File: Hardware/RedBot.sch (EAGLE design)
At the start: 64 parts, among them U1 ATMEGA328P, U2 TB6612FNG, U3 MIC5219 5V, U4 MIC5219 3.3V, U5 FT232RLSSOP, U6 7408SE, Y1 16MHz

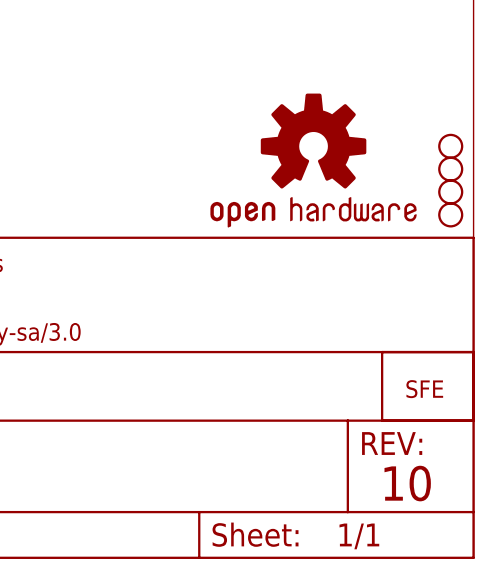
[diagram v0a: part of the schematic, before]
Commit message: Production readied
add fiducials & create panel
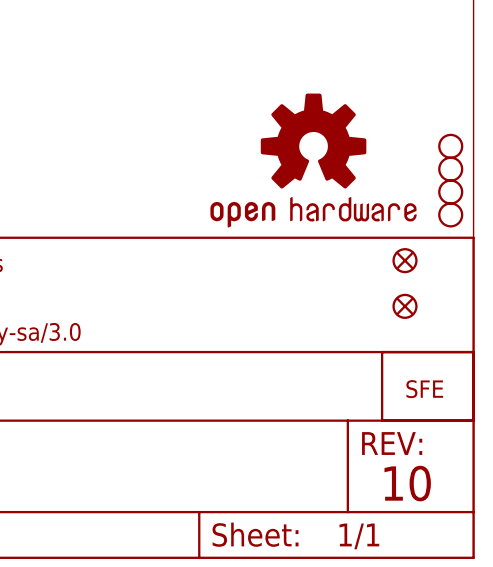
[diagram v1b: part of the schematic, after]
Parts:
- added FID1, FID2: FIDUCIALUFIDUCIAL, SparkFun-Aesthetics:FIDUCIALUFIDUCIAL
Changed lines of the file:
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@@
 <part name="U$20" library="SparkFun-Aesthetics" deviceset="5V" device=""/>
 <part name="U$21" library="SparkFun-Aesthetics" deviceset="FOUR_LAYER_WARNING" device=""/>
+<part name="FID1" library="SparkFun-Aesthetics" deviceset="FIDUCIAL" device="UFIDUCIAL"/>
+<part name="FID2" library="SparkFun-Aesthetics" deviceset="FIDUCIAL" device="UFIDUCIAL"/>
 </parts>
 <sheets>
@@
 <instance part="U$20" gate="G$1" x="127" y="165.1"/>
 <instance part="U$21" gate="G$1" x="304.8" y="36.068"/>
+<instance part="FID1" gate="G$1" x="398.78" y="33.02"/>
+<instance part="FID2" gate="G$1" x="398.78" y="27.94"/>
 </instances>
 <busses>

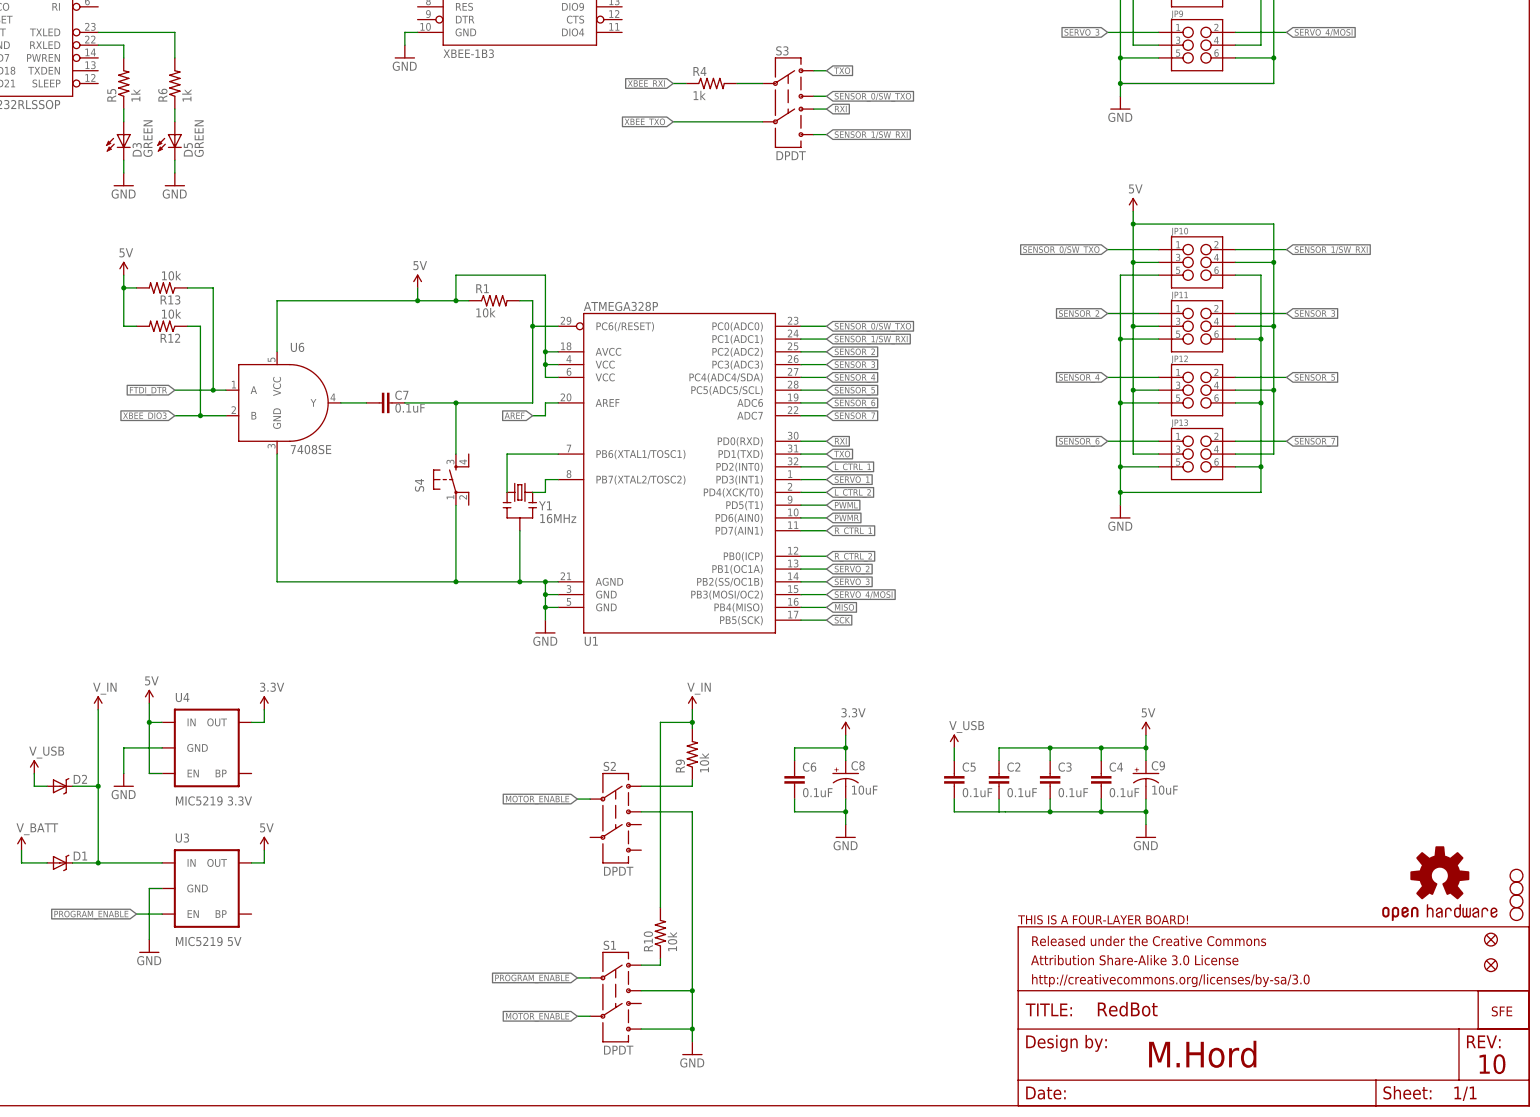
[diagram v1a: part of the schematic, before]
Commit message: Fix polarity issue on FT232 LEDs
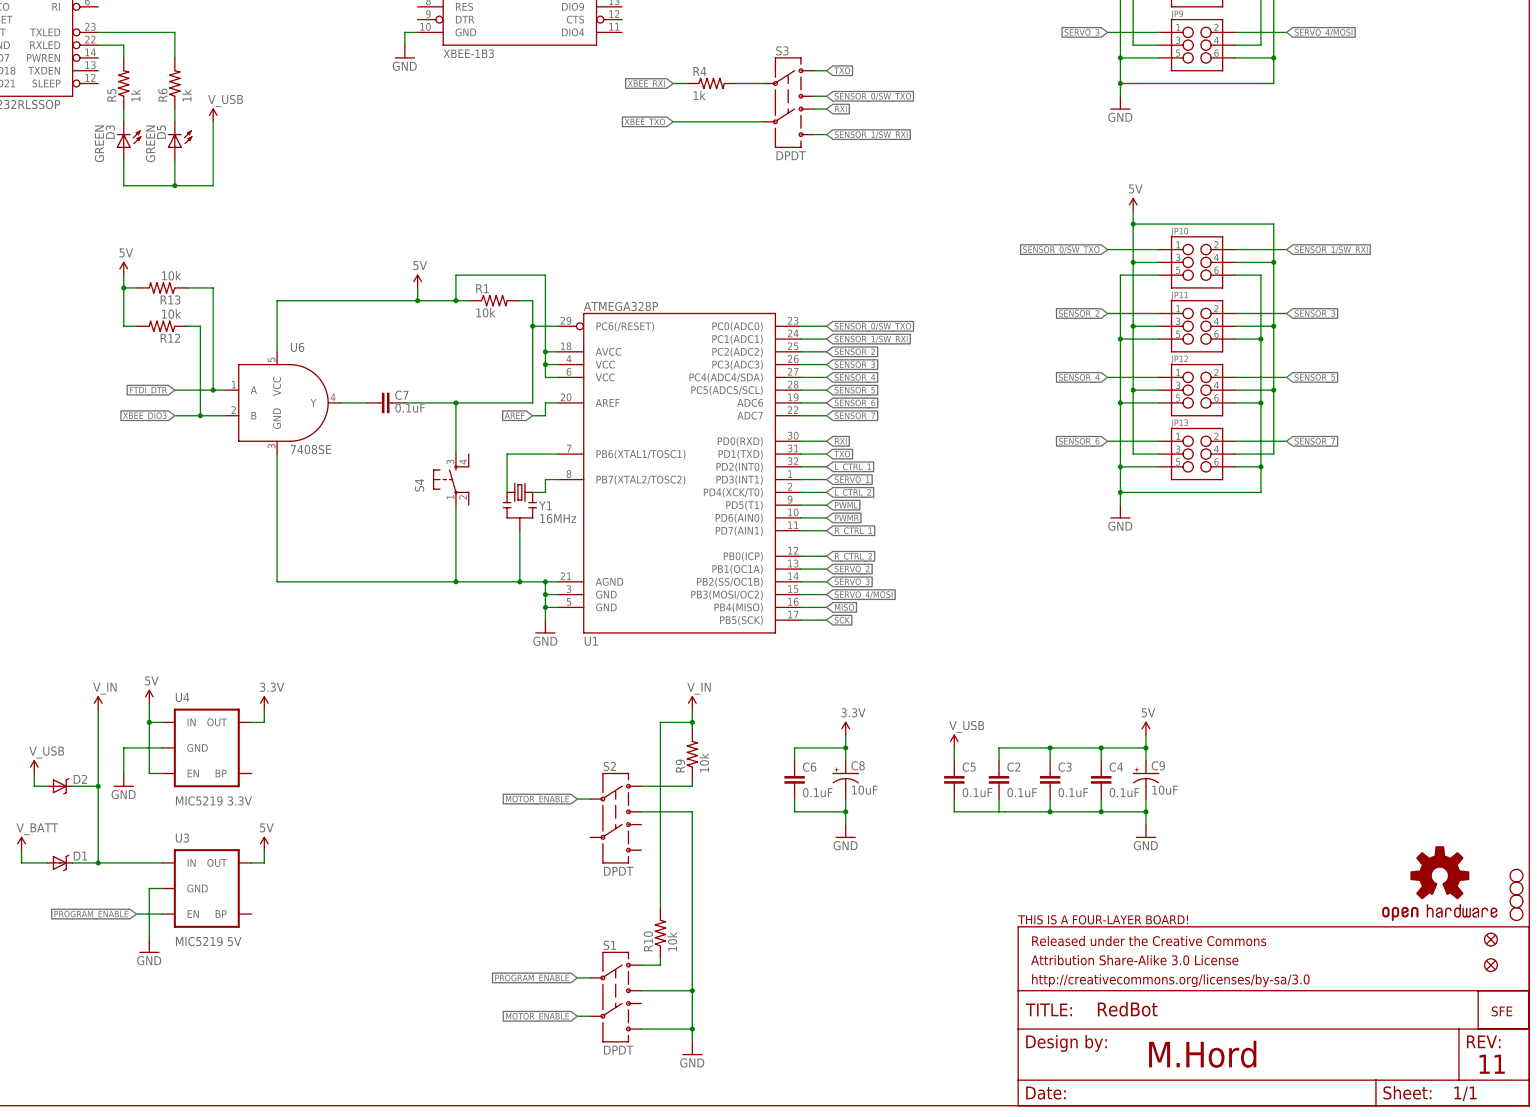
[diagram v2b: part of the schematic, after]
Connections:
- net GND: no longer D3.C, D5.C
- net N$3: now also D5.C; no longer D5.A
- net N$4: now also D3.C; no longer D3.A
- net V_USB: now also D3.A, D5.A
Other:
- note added: "11"
- note removed: "10"
- moved on the sheet: D3, D5
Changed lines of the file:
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@@
 <attribute name="VALUE" value="GREEN"/>
 </part>
-<part name="GND12" library="SparkFun-Aesthetics" deviceset="GND" device=""/>
-<part name="GND13" library="SparkFun-Aesthetics" deviceset="GND" device=""/>
 <part name="JP5" library="SparkFun-Connectors" deviceset="AVR_SPI_PRG_6" device="PTH" value="AVR_SPI_PRG_6PTH"/>
 <part name="GND15" library="SparkFun-Aesthetics" deviceset="GND" device=""/>
@@
 <part name="FID1" library="SparkFun-Aesthetics" deviceset="FIDUCIAL" device="UFIDUCIAL"/>
 <part name="FID2" library="SparkFun-Aesthetics" deviceset="FIDUCIAL" device="UFIDUCIAL"/>
+<part name="U$22" library="SparkFun-Aesthetics" deviceset="5V" device="" value="V_USB"/>
 </parts>
 <sheets>
@@
 <wire x1="0" y1="254" x2="0" y2="0" width="0.1524" layer="94"/>
 <text x="330.2" y="7.62" size="5.08" layer="94">M.Hord</text>
-<text x="395.986" y="6.35" size="3.81" layer="94">10</text>
+<text x="395.986" y="6.35" size="3.81" layer="94">11</text>
 </plain>
 <instances>
@@
 <instance part="U$10" gate="G$1" x="185.42" y="162.56"/>
 <instance part="S4" gate="S" x="193.04" y="124.46" rot="R90"/>
-<instance part="D3" gate="G$1" x="127" y="193.04"/>
+<instance part="D3" gate="G$1" x="127" y="190.5" rot="R180"/>
 <instance part="D4" gate="G$1" x="35.56" y="243.84" rot="R90"/>
 <instance part="R5" gate="G$1" x="127" y="203.2" rot="R90"/>
 <instance part="R6" gate="G$1" x="137.16" y="203.2" rot="R90"/>
 <instance part="R7" gate="G$1" x="25.4" y="243.84" rot="R180"/>
-<instance part="D5" gate="G$1" x="137.16" y="193.04"/>
-<instance part="GND12" gate="1" x="137.16" y="182.88"/>
-<instance part="GND13" gate="1" x="127" y="182.88"/>
+<instance part="D5" gate="G$1" x="137.16" y="190.5" rot="R180"/>
 <instance part="JP5" gate="G$1" x="27.94" y="205.74" smashed="yes">
 <attribute name="NAME" x="23.622" y="211.582" size="1.778" layer="95"/>
@@
 <instance part="FID1" gate="G$1" x="398.78" y="33.02"/>
 <instance part="FID2" gate="G$1" x="398.78" y="27.94"/>
+<instance part="U$22" gate="G$1" x="144.78" y="195.58"/>
 </instances>
 <busses>
@@
 </segment>
 <segment>
-<pinref part="D3" gate="G$1" pin="C"/>
-<pinref part="GND13" gate="1" pin="GND"/>
-<wire x1="127" y1="187.96" x2="127" y2="185.42" width="0.1524" layer="91"/>
-</segment>
-<segment>
-<pinref part="D5" gate="G$1" pin="C"/>
-<pinref part="GND12" gate="1" pin="GND"/>
-<wire x1="137.16" y1="187.96" x2="137.16" y2="185.42" width="0.1524" layer="91"/>
-</segment>
-<segment>
 <pinref part="JP5" gate="G$1" pin="6"/>
 <wire x1="38.1" y1="203.2" x2="40.64" y2="203.2" width="0.1524" layer="91"/>
@@
 <wire x1="292.1" y1="71.12" x2="292.1" y2="68.58" width="0.1524" layer="91"/>
 </segment>
+<segment>
+<pinref part="D3" gate="G$1" pin="A"/>
+<wire x1="127" y1="187.96" x2="127" y2="182.88" width="0.1524" layer="91"/>
+<pinref part="D5" gate="G$1" pin="A"/>
+<wire x1="127" y1="182.88" x2="137.16" y2="182.88" width="0.1524" layer="91"/>
+<wire x1="137.16" y1="182.88" x2="137.16" y2="187.96" width="0.1524" layer="91"/>
+<pinref part="U$22" gate="G$1" pin="5V"/>
+<wire x1="137.16" y1="182.88" x2="144.78" y2="182.88" width="0.1524" layer="91"/>
+<wire x1="144.78" y1="182.88" x2="144.78" y2="195.58" width="0.1524" layer="91"/>
+<junction x="137.16" y="182.88"/>
+</segment>
 </net>
 <net name="PROGRAM_ENABLE" class="0">
@@
 <wire x1="210.82" y1="137.16" x2="208.28" y2="137.16" width="0.1524" layer="91"/>
 <label x="208.28" y="137.16" size="1.27" layer="95" rot="R180" xref="yes"/>
-</segment>
-</net>
-<net name="N$3" class="0">
-<segment>
-<pinref part="R6" gate="G$1" pin="1"/>
-<pinref part="D5" gate="G$1" pin="A"/>
-<wire x1="137.16" y1="198.12" x2="137.16" y2="195.58" width="0.1524" layer="91"/>
-</segment>
-</net>
-<net name="N$4" class="0">
-<segment>
-<pinref part="R5" gate="G$1" pin="1"/>
-<pinref part="D3" gate="G$1" pin="A"/>
-<wire x1="127" y1="198.12" x2="127" y2="195.58" width="0.1524" layer="91"/>
 </segment>
 </net>
@@
 </segment>
 </net>
+<net name="N$3" class="0">
+<segment>
+<pinref part="D5" gate="G$1" pin="C"/>
+<pinref part="R6" gate="G$1" pin="1"/>
+<wire x1="137.16" y1="195.58" x2="137.16" y2="198.12" width="0.1524" layer="91"/>
+</segment>
+</net>
+<net name="N$4" class="0">
+<segment>
+<pinref part="R5" gate="G$1" pin="1"/>
+<pinref part="D3" gate="G$1" pin="C"/>
+<wire x1="127" y1="198.12" x2="127" y2="195.58" width="0.1524" layer="91"/>
+</segment>
+</net>

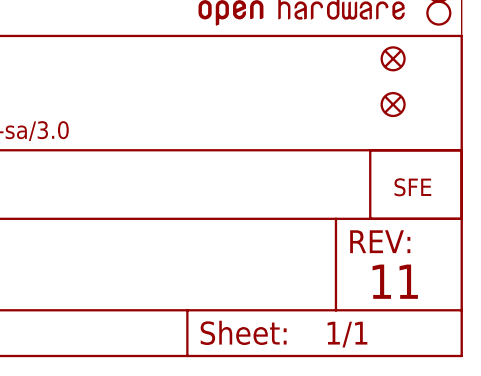
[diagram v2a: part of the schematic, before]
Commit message: Update parts to 0603
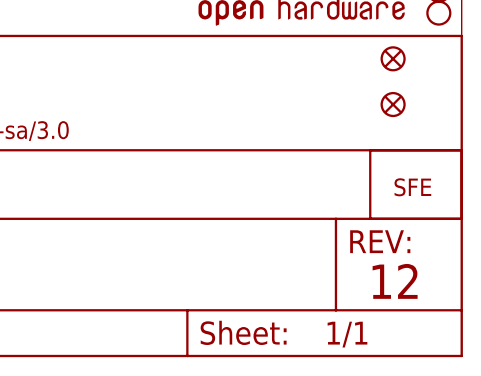
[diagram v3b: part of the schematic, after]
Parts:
- C2, C3, C4, C5, C6, C7: device SparkFun-Capacitors:.1UF-CER -> SparkFun-Capacitors:0.1UF-25V(+80/-20%)(0603)
- R1: device SparkFun-Resistors:10KOHM1/10W1%(0603) -> SparkFun-Resistors:10KOHM1/10W1%(0603)0603
- R10, R11, R12, R13, R9: device SparkFun-Resistors:10KOHM1/10W1%(0603) -> SparkFun-Resistors:10KOHM1/10W1%(0603)0603; VALUE 10k -> (none)
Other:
- note added: "12"
- note removed: "11"
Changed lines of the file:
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@@
 <part name="FRAME1" library="SparkFun-Aesthetics" deviceset="FRAME-LETTER" device=""/>
 <part name="U1" library="SparkFun-DigitalIC" deviceset="ATMEGA328_SMT" device="" value="ATMEGA328P"/>
-<part name="C2" library="SparkFun-Capacitors" deviceset=".1UF-CER" device="" value="0.1uF"/>
-<part name="C3" library="SparkFun-Capacitors" deviceset=".1UF-CER" device="" value="0.1uF"/>
-<part name="R1" library="SparkFun-Resistors" deviceset="10KOHM1/10W1%(0603)" device="" value="10k"/>
+<part name="C2" library="SparkFun-Capacitors" deviceset="0.1UF-25V(+80/-20%)(0603)" device="" value="0.1uF"/>
+<part name="C3" library="SparkFun-Capacitors" deviceset="0.1UF-25V(+80/-20%)(0603)" device="" value="0.1uF"/>
+<part name="R1" library="SparkFun-Resistors" deviceset="10KOHM1/10W1%(0603)" device="0603" value="10k"/>
 <part name="U5" library="SparkFun-DigitalIC" deviceset="FT232RL" device="SSOP"/>
 <part name="U2" library="SparkFun-PowerIC" deviceset="TB6621FNG" device="" value="TB6612FNG"/>
 <part name="JP3" library="SparkFun-Connectors" deviceset="POWER_JACK" device="SMD" value="5.5x2.1mm Barrel"/>
-<part name="C4" library="SparkFun-Capacitors" deviceset=".1UF-CER" device="" value="0.1uF"/>
-<part name="C5" library="SparkFun-Capacitors" deviceset=".1UF-CER" device="" value="0.1uF"/>
-<part name="C6" library="SparkFun-Capacitors" deviceset=".1UF-CER" device="" value="0.1uF"/>
+<part name="C4" library="SparkFun-Capacitors" deviceset="0.1UF-25V(+80/-20%)(0603)" device="" value="0.1uF"/>
+<part name="C5" library="SparkFun-Capacitors" deviceset="0.1UF-25V(+80/-20%)(0603)" device="" value="0.1uF"/>
+<part name="C6" library="SparkFun-Capacitors" deviceset="0.1UF-25V(+80/-20%)(0603)" device="" value="0.1uF"/>
 <part name="S1" library="SparkFun-Electromechanical" deviceset="SWITCH-DPDT" device="AYZ0202" value="DPDT"/>
 <part name="S2" library="SparkFun-Electromechanical" deviceset="SWITCH-DPDT" device="AYZ0202" value="DPDT"/>
@@
 <part name="GND11" library="SparkFun-Aesthetics" deviceset="GND" device=""/>
 <part name="U$9" library="SparkFun-Aesthetics" deviceset="5V" device=""/>
-<part name="C7" library="SparkFun-Capacitors" deviceset=".1UF-CER" device="" value="0.1uF">
+<part name="C7" library="SparkFun-Capacitors" deviceset="0.1UF-25V(+80/-20%)(0603)" device="" value="0.1uF">
 <attribute name="PROD_ID" value="CAP-00810"/>
 <attribute name="VALUE" value="0.1uF"/>
@@
 <part name="U$13" library="SparkFun-Aesthetics" deviceset="5V" device=""/>
 <part name="V_IN1" library="SparkFun-Aesthetics" deviceset="5V" device="" value="V_IN"/>
-<part name="R9" library="SparkFun-Resistors" deviceset="10KOHM1/10W1%(0603)" device="" value="10k">
+<part name="R9" library="SparkFun-Resistors" deviceset="10KOHM1/10W1%(0603)" device="0603" value="10k">
 <attribute name="PROD_ID" value="RES-00824"/>
-<attribute name="VALUE" value="10k"/>
 </part>
-<part name="R10" library="SparkFun-Resistors" deviceset="10KOHM1/10W1%(0603)" device="" value="10k">
+<part name="R10" library="SparkFun-Resistors" deviceset="10KOHM1/10W1%(0603)" device="0603" value="10k">
 <attribute name="PROD_ID" value="RES-00824"/>
-<attribute name="VALUE" value="10k"/>
 </part>
 <part name="U$14" library="SparkFun-Aesthetics" deviceset="5V" device=""/>
@@
 <part name="Q1" library="SparkFun-DiscreteSemi" deviceset="IRF7509" device=""/>
 <part name="GND19" library="SparkFun-Aesthetics" deviceset="GND" device=""/>
-<part name="R11" library="SparkFun-Resistors" deviceset="10KOHM1/10W1%(0603)" device="" value="10k">
+<part name="R11" library="SparkFun-Resistors" deviceset="10KOHM1/10W1%(0603)" device="0603" value="10k">
 <attribute name="PROD_ID" value="RES-00824"/>
-<attribute name="VALUE" value="10k"/>
 </part>
 <part name="U$18" library="SparkFun-Aesthetics" deviceset="V_BATT" device=""/>
@@
 <part name="U$19" library="SparkFun-Aesthetics" deviceset="5V" device="" value="V_USB"/>
 <part name="U6" library="SparkFun-DigitalIC" deviceset="74*08" device="SE"/>
-<part name="R12" library="SparkFun-Resistors" deviceset="10KOHM1/10W1%(0603)" device="" value="10k">
+<part name="R12" library="SparkFun-Resistors" deviceset="10KOHM1/10W1%(0603)" device="0603" value="10k">
 <attribute name="PROD_ID" value="RES-00824"/>
-<attribute name="VALUE" value="10k"/>
 </part>
-<part name="R13" library="SparkFun-Resistors" deviceset="10KOHM1/10W1%(0603)" device="" value="10k">
+<part name="R13" library="SparkFun-Resistors" deviceset="10KOHM1/10W1%(0603)" device="0603" value="10k">
 <attribute name="PROD_ID" value="RES-00824"/>
-<attribute name="VALUE" value="10k"/>
 </part>
 <part name="U$20" library="SparkFun-Aesthetics" deviceset="5V" device=""/>
@@
 <wire x1="0" y1="254" x2="0" y2="0" width="0.1524" layer="94"/>
 <text x="330.2" y="7.62" size="5.08" layer="94">M.Hord</text>
-<text x="395.986" y="6.35" size="3.81" layer="94">11</text>
+<text x="395.986" y="6.35" size="3.81" layer="94">12</text>
 </plain>
 <instances>
